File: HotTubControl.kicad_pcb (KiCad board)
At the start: 2 copper layers, 90 x 90 mm, 27 parts, among them J1 Wasser Vorlauf, J2 Wasser Rücklauf, J3 Massagepumpe, J4 Filterpumpe, J5 Füllstandsensor, J6 Conn_01x03, K1 JV-KT, Q1 BC337, Q2 BSS138

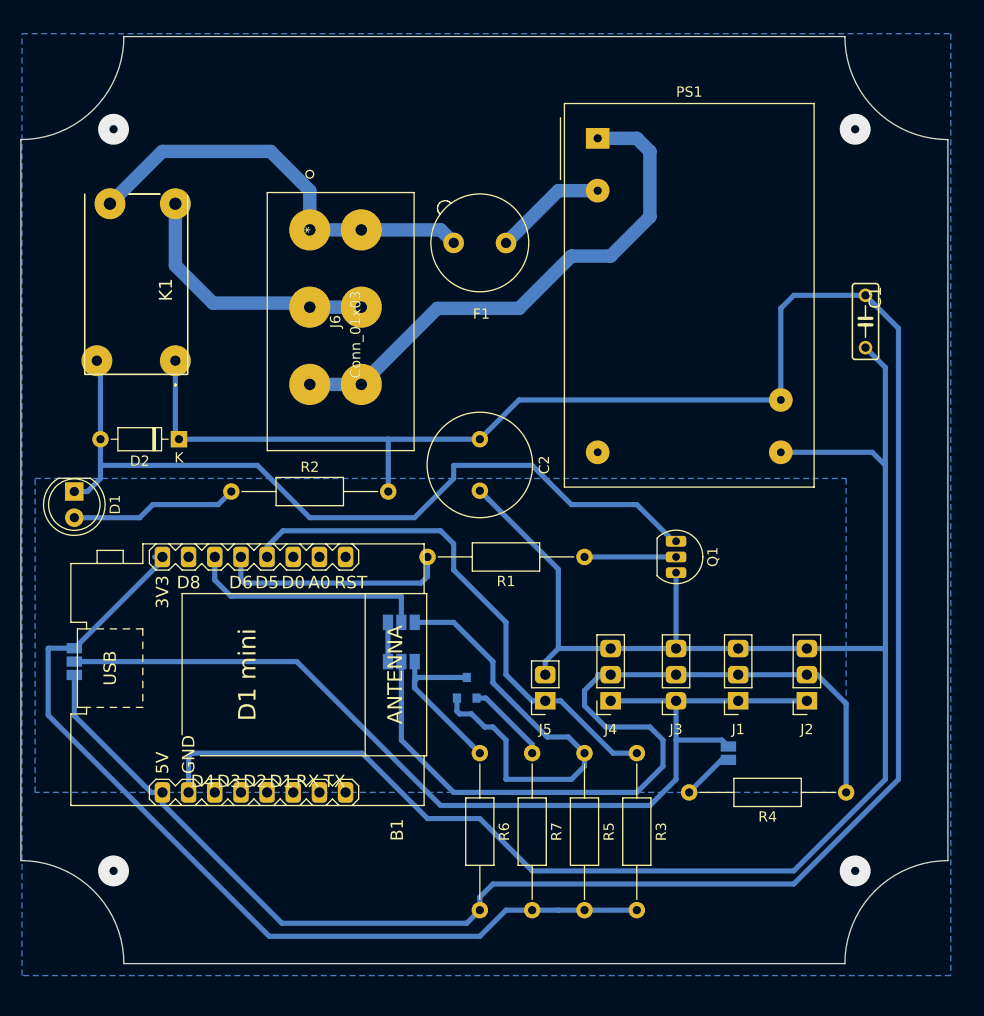
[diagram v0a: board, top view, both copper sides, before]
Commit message: V2.0 added one channesl
Ein zweiter Relaiskanal zu Steuerung der  Massagepumpe wurde integriert
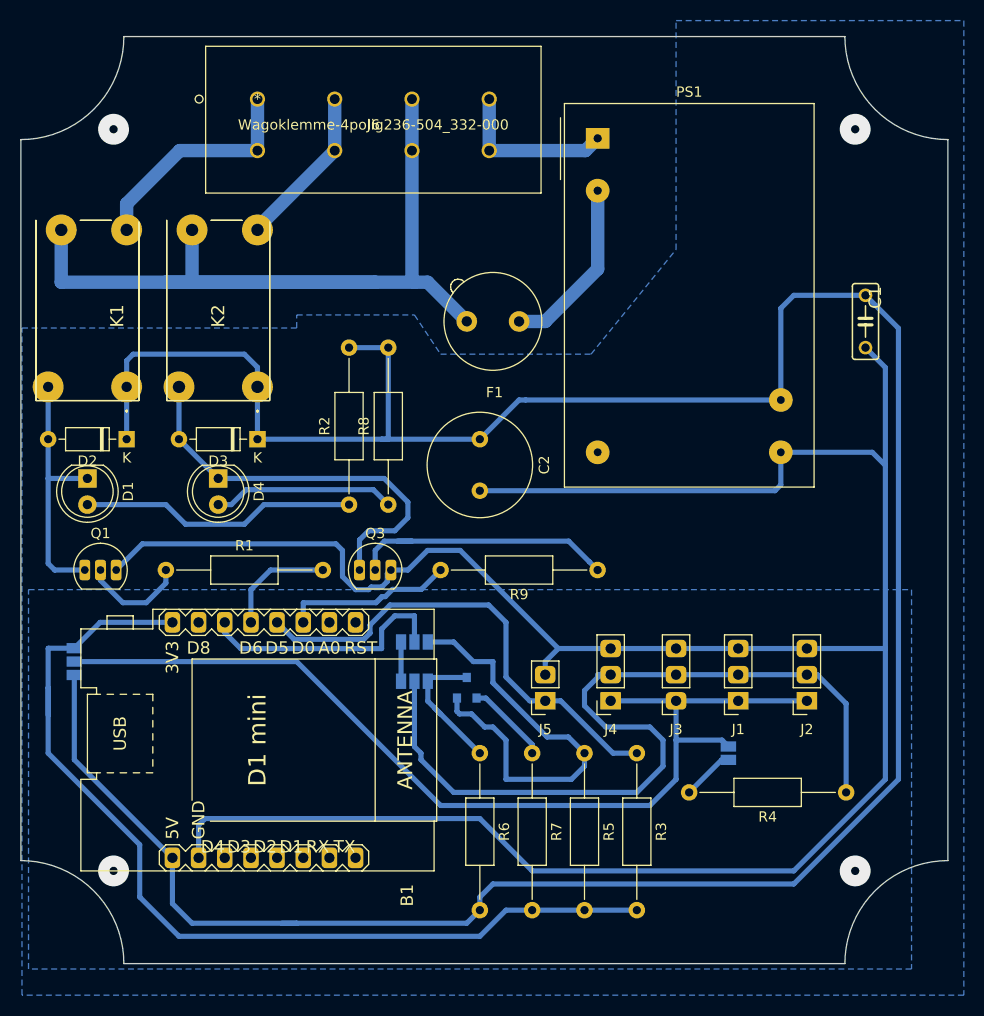
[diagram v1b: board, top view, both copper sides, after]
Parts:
- added D3: 1N4148, Diode_THT:D_DO-35_SOD27_P7.62mm_Horizontal, F.Cu at (79.2, 96.4)
- added D4: LED, LED_THT:LED_D5.0mm, F.Cu at (75.4, 100.2)
- added K2: JV-KT, SamacSys_Parts:JV24SKT, F.Cu at (79.2, 91.4)
- added Q3: BC337, Package_TO_SOT_THT:TO-92_Inline, F.Cu at (89.4, 109.1)
- added R8: R380, Resistor_THT:R_Axial_DIN0207_L6.3mm_D2.5mm_P15.24mm_Horizontal, F.Cu at (92.0, 102.8)
- added R9: 10k, Resistor_THT:R_Axial_DIN0207_L6.3mm_D2.5mm_P15.24mm_Horizontal, F.Cu at (112.3, 109.1)
- J6: value Conn_01x03 -> Wagoklemme-4polig236-504_332-000; footprint ene9ba_footprint:236-503 -> ene9ba_footprint:WAGOKlemme4pol
- moved Q1 57.2 mm to (62.7, 109.1), turned to 0 degrees
- moved R1 40.7 mm to (70.4, 109.1), turned to 0 degrees
- moved J6 13.7 mm to (79.2, 63.4), turned to 0 degrees
- moved R2 11.5 mm to (88.1, 102.8), turned to 90 degrees
- moved F1 7.73 mm to (104.7, 85.0)
- moved B1 6.42 mm to (79.2, 125.7)
- moved K1 5.37 mm to (66.5, 91.4)
- moved D2 5.08 mm to (66.5, 96.4)
- moved JP1 2.29 mm to (94.5, 116.1)
- moved JP2 2.29 mm to (94.5, 119.9)
- moved D1 1.80 mm to (62.7, 100.2)
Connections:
- B1 pad JP1.3: (no net) -> Net-(B1-PadJP1.3)
- J6 pad 1: Net-(F1-Pad2) -> Net-(J6-Pad1)
- J6 pad 2: Net-(J6-Pad2) -> Net-(J6-Pad1)
- K1 pad 2: Net-(J6-Pad2) -> Net-(J6-Pad1)
- PS1 pad 1: Net-(J6-Pad3) -> Net-(J6-Pad7)
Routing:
- net GND: track 194.0 -> 251.3 mm
- net Net-(D1-Pad1): track 78.6 -> 24.8 mm
- net Net-(F1-Pad2): track 41.4 -> 89.3 mm
- net Net-(D3-Pad2): track 0.00 -> 40.5 mm
- net Net-(J6-Pad3): track 51.7 -> 15.8 mm
- net Net-(Q3-Pad2): track 0.00 -> 27.0 mm
- net +5V: track 238.3 -> 265.2 mm
- net Net-(J6-Pad2): track 25.7 -> 0.00 mm
- net Net-(J6-Pad1): track 0.00 -> 22.4 mm
- net Net-(D4-Pad2): track 0.00 -> 17.7 mm
- net Net-(B1-PadJP1.3): track 0.00 -> 17.2 mm
- net Net-(J6-Pad7): track 0.00 -> 16.0 mm
- net Net-(B1-PadJP1.5): track 22.6 -> 10.9 mm
- net Net-(D1-Pad2): track 16.3 -> 27.0 mm
- net Net-(F1-Pad1): track 11.0 -> 17.3 mm
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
